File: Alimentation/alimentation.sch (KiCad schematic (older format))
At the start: 0 parts

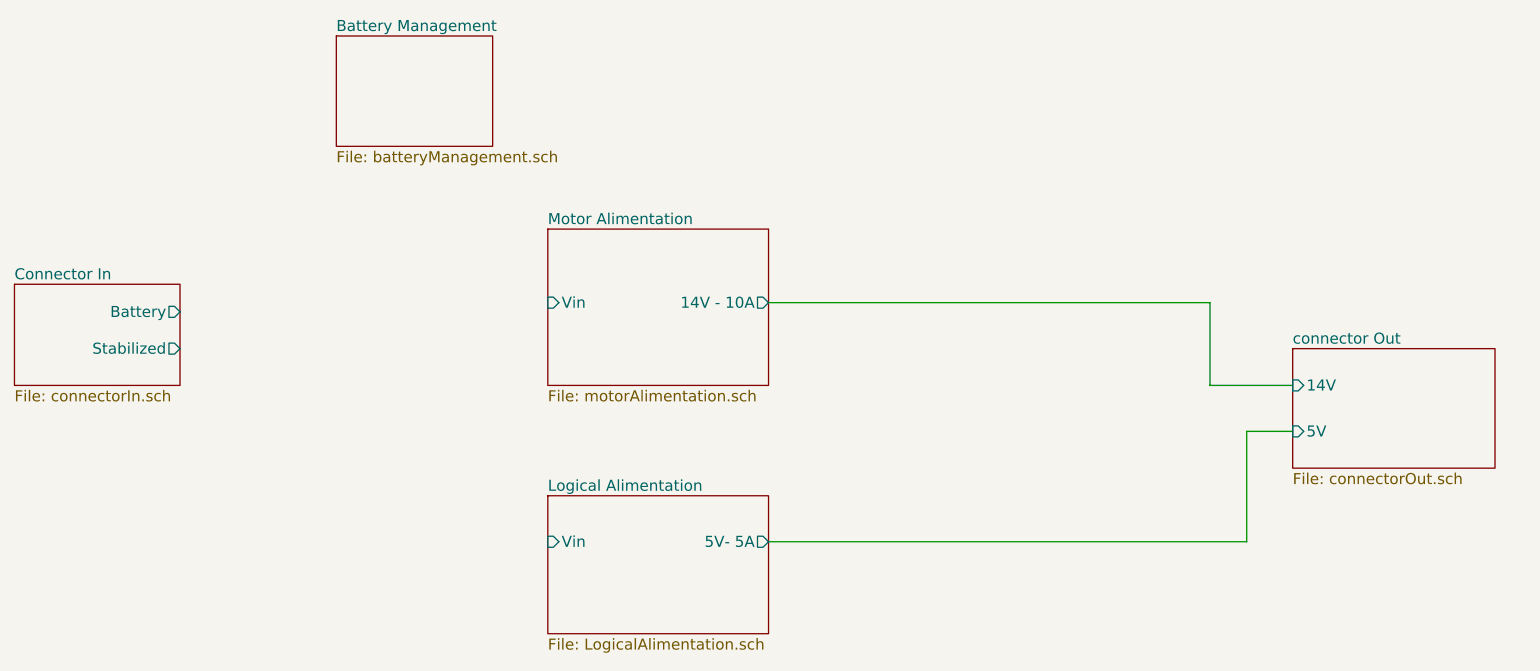
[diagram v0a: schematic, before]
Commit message: Adding board for alimentation
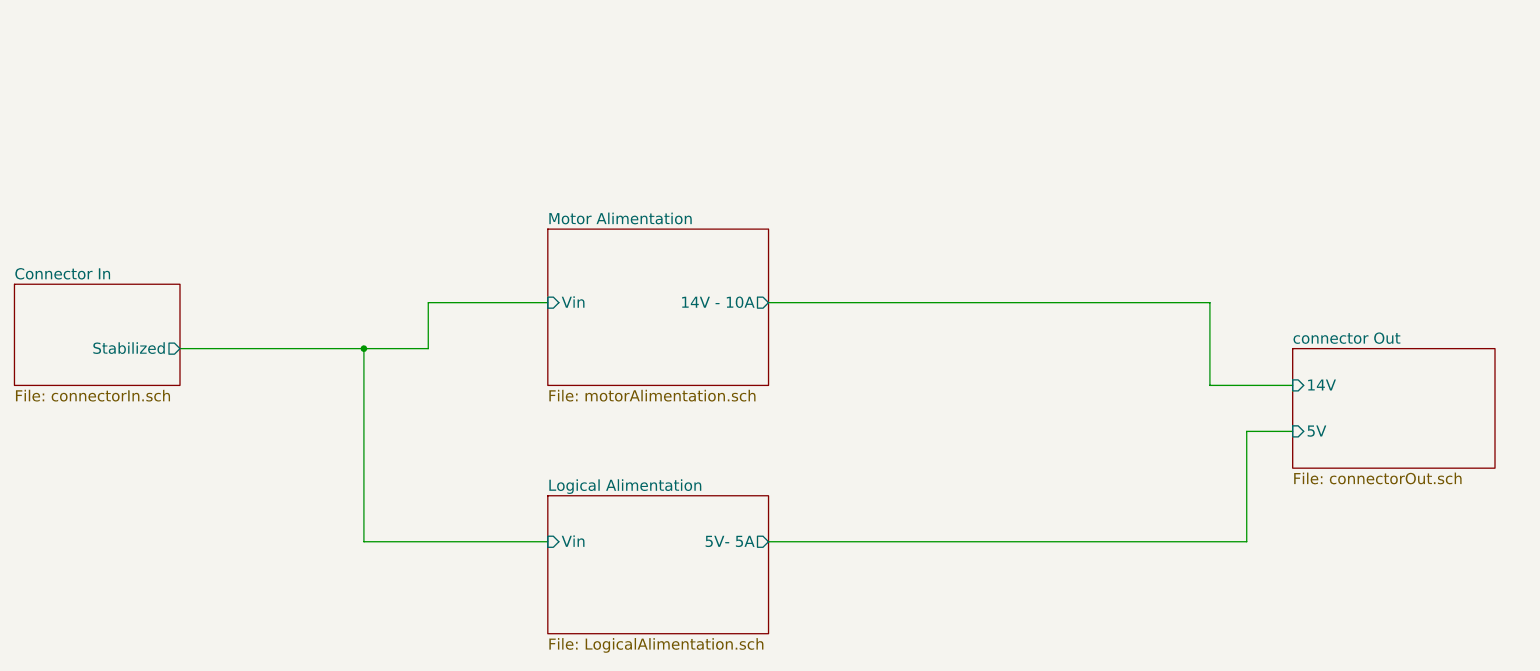
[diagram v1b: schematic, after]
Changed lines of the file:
@@
-EESchema Schematic File Version 2  date Thu 13 Mar 2014 12:12:56 CET
+EESchema Schematic File Version 2
 LIBS:power
 LIBS:device
@@
 LIBS:perso
 LIBS:alimentation-cache
-EELAYER 25  0
+EELAYER 24 0
 EELAYER END
-$Descr A4 11700 8267
+$Descr A4 11693 8268
 encoding utf-8
-Sheet 1 7
+Sheet 1 5
 Title ""
-Date "13 mar 2014"
+Date "20 mar 2014"
 Rev ""
 Comp ""
@@
 Comment4 ""
 $EndDescr
+Connection ~ 4250 2650
+Wire Wire Line
+	4250 2650 4250 3700
+Wire Wire Line
+	4250 3700 5250 3700
 Wire Wire Line
 	9300 2850 8850 2850
@@
 Wire Wire Line
 	9050 3100 9300 3100
+Wire Wire Line
+	5250 2400 4600 2400
+Wire Wire Line
+	4600 2400 4600 2650
+Wire Wire Line
+	4600 2650 3250 2650
 $Sheet
 S 9300 2650 1100 650
@@
 $EndSheet
 $Sheet
-S 4100 950  850  600
-U 53147D44
-F0 "Battery Management" 60
-F1 "batteryManagement.sch" 60
-$EndSheet
-$Sheet
 S 2350 2300 900  550
 U 53147D23
 F0 "Connector In" 60
 F1 "connectorIn.sch" 60
-F2 "Battery" O R 3250 2450 60
 F3 "Stabilized" O R 3250 2650 60
 $EndSheet
